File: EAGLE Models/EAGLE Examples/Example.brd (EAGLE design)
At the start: 160 x 100 mm, 2 parts

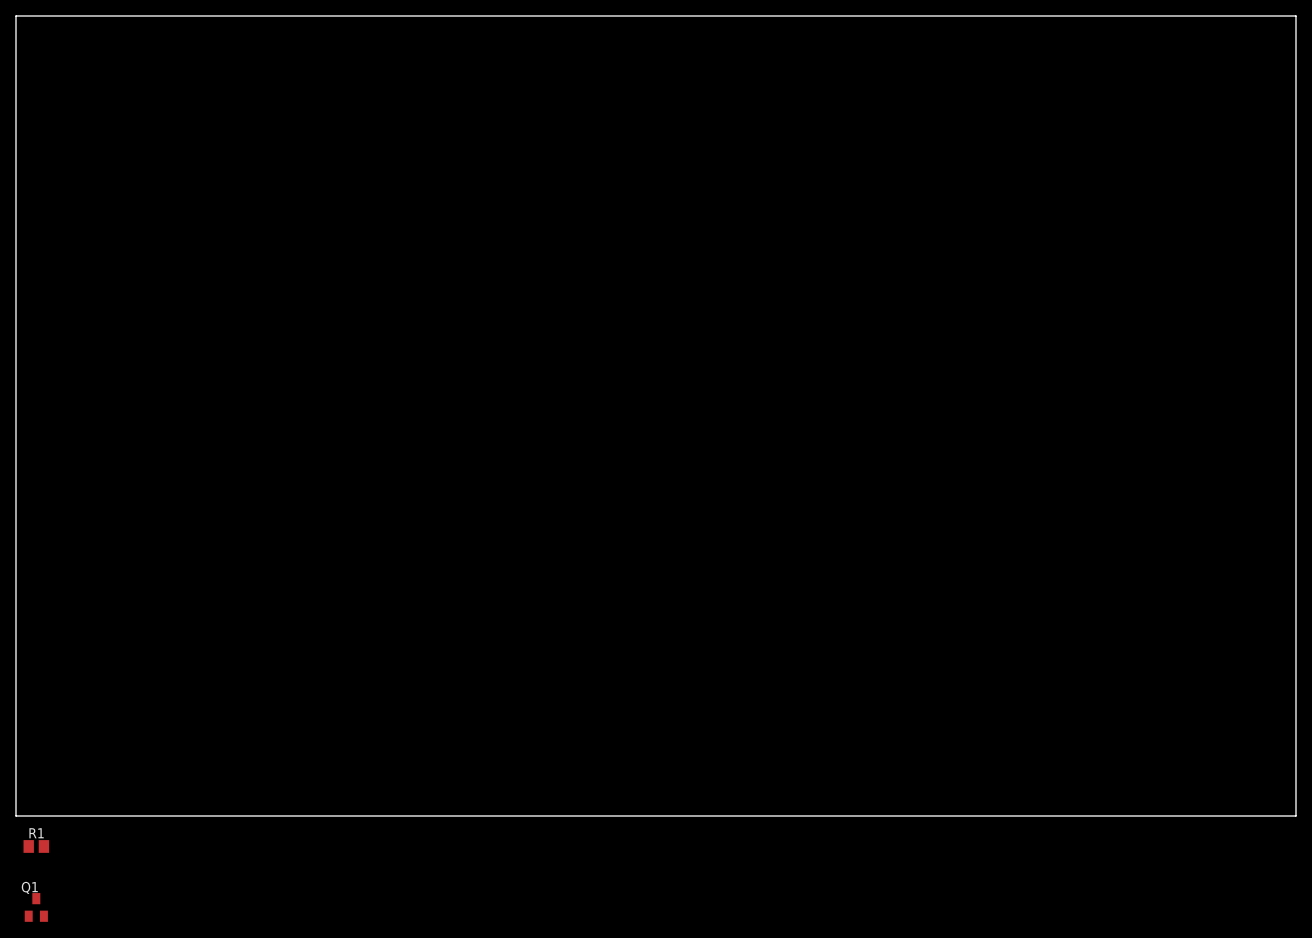
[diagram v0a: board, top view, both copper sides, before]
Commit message: Finished Example board for EAGLE tutorial
Did board layout
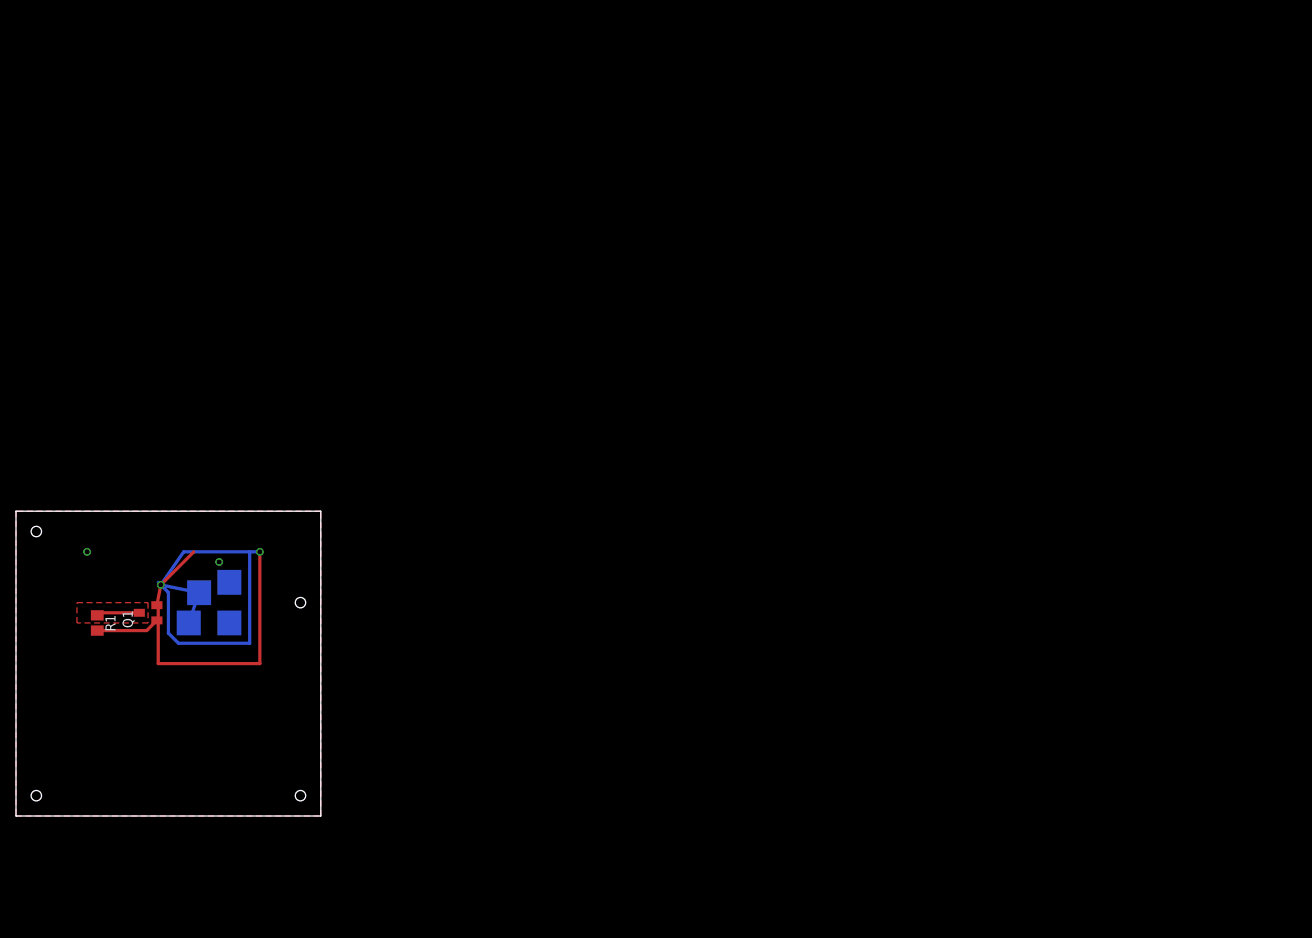
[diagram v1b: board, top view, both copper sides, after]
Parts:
- added D1: OVSA1BBC, TTelectronics:4-PLCC
- moved Q1 39.4 mm to (16.5, 25.4), turned to 90 degrees
- moved R1 29.0 mm to (10.2, 24.1), turned to 270 degrees
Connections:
- net N$1 renamed GATE
- removed net N$2: Q1.3
- removed net N$3: Q1.2
- new net DRIN: D1.1, D1.2, Q1.2
- new net GND: D1.3, D1.4
- new net VCC: Q1.3, R1.1
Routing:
- net DRIN: track 0.00 -> 95.1 mm, vias 0 -> 2
- net GATE: track 0.00 -> 7.98 mm
- net VCC: track 0.00 -> 5.38 mm
- added copper zone on layer 1, net GND
- added copper zone on layer 16, net GND
- added copper zone on layer 1, net VCC
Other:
- board size 160 x 100 mm -> 38.1 x 38.1 mm
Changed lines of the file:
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@@
 <layer number="43" name="vRestrict" color="2" fill="10" visible="yes" active="yes"/>
 <layer number="44" name="Drills" color="7" fill="1" visible="no" active="yes"/>
-<layer number="45" name="Holes" color="7" fill="1" visible="no" active="yes"/>
+<layer number="45" name="Holes" color="7" fill="1" visible="yes" active="yes"/>
 <layer number="46" name="Milling" color="3" fill="1" visible="no" active="yes"/>
 <layer number="47" name="Measures" color="7" fill="1" visible="no" active="yes"/>
@@
 <board>
 <plain>
-<wire x1="0" y1="0" x2="160" y2="0" width="0" layer="20"/>
-<wire x1="160" y1="0" x2="160" y2="100" width="0" layer="20"/>
-<wire x1="160" y1="100" x2="0" y2="100" width="0" layer="20"/>
-<wire x1="0" y1="100" x2="0" y2="0" width="0" layer="20"/>
+<wire x1="0" y1="0" x2="38.1" y2="0" width="0" layer="20"/>
+<wire x1="38.1" y1="0" x2="38.1" y2="38.1" width="0" layer="20"/>
+<wire x1="38.1" y1="38.1" x2="0" y2="38.1" width="0" layer="20"/>
+<wire x1="0" y1="38.1" x2="0" y2="0" width="0" layer="20"/>
+<hole x="2.54" y="35.56" drill="1.3"/>
+<hole x="2.54" y="2.54" drill="1.3"/>
+<hole x="35.56" y="2.54" drill="1.3"/>
+<hole x="35.56" y="26.67" drill="1.3"/>
 </plain>
 <attributes>
@@
 </autorouter>
 <elements>
-<element name="R1" library="adafruit" package="M0805" value="5K" x="2.54" y="-3.81"/>
-<element name="Q1" library="adafruit" package="SOT23" value="" x="2.54" y="-11.43"/>
+<element name="R1" library="adafruit" package="M0805" value="5K" x="10.16" y="24.13" rot="R270"/>
+<element name="Q1" library="adafruit" package="SOT23" value="" x="16.51" y="25.4" rot="R90"/>
+<element name="D1" library="TTelectronics" package="4-PLCC" value="OVSA1BBC" x="24.13" y="26.67" rot="MR270"/>
 </elements>
 <signals>
-<signal name="N$1">
+<signal name="GATE">
 <contactref element="R1" pad="2"/>
 <contactref element="Q1" pad="1"/>
-<wire x1="3.49" y1="-3.81" x2="1.59" y2="-12.53" width="0" layer="19" extent="1-1"/>
+<wire x1="10.16" y1="23.18" x2="16.34" y2="23.18" width="0.4064" layer="1"/>
+<wire x1="16.34" y1="23.18" x2="17.61" y2="24.45" width="0.4064" layer="1"/>
 </signal>
-<signal name="N$2">
+<signal name="DRIN">
+<contactref element="Q1" pad="2"/>
+<contactref element="D1" pad="2"/>
+<contactref element="D1" pad="1"/>
+<wire x1="17.61" y1="26.35" x2="18.1" y2="28.89" width="0.4064" layer="1"/>
+<wire x1="18.1" y1="28.89" x2="22.89" y2="27.91" width="0.4064" layer="16"/>
+<wire x1="22.89" y1="27.91" x2="21.59" y2="24.13" width="0.4064" layer="16"/>
+<via x="18.1" y="28.89" extent="1-16" drill="0.6" shape="square"/>
+<wire x1="18.1" y1="28.89" x2="22.23" y2="33.02" width="0.4064" layer="1"/>
+<wire x1="30.48" y1="33.02" x2="30.48" y2="19.05" width="0.4064" layer="1"/>
+<wire x1="30.48" y1="19.05" x2="17.78" y2="19.05" width="0.4064" layer="1"/>
+<wire x1="17.78" y1="19.05" x2="17.78" y2="26.67" width="0.4064" layer="1"/>
+<wire x1="18.1" y1="28.89" x2="20.96" y2="33.02" width="0.4064" layer="16"/>
+<wire x1="20.96" y1="33.02" x2="29.21" y2="33.02" width="0.4064" layer="16"/>
+<wire x1="29.21" y1="33.02" x2="29.21" y2="21.59" width="0.4064" layer="16"/>
+<wire x1="29.21" y1="21.59" x2="20.32" y2="21.59" width="0.4064" layer="16"/>
+<wire x1="20.32" y1="21.59" x2="19.05" y2="22.86" width="0.4064" layer="16"/>
+<wire x1="19.05" y1="22.86" x2="19.05" y2="27.94" width="0.4064" layer="16"/>
+<wire x1="19.05" y1="27.94" x2="17.78" y2="29.21" width="0.4064" layer="16"/>
+<via x="30.48" y="33.02" extent="1-16" drill="0.6"/>
+<wire x1="30.48" y1="33.02" x2="29.21" y2="33.02" width="0.4064" layer="16"/>
+</signal>
+<signal name="GND">
+<contactref element="D1" pad="4"/>
+<contactref element="D1" pad="3"/>
+<polygon width="0.4064" layer="1" rank="6">
+<vertex x="0" y="0"/>
+<vertex x="38.1" y="0"/>
+<vertex x="38.1" y="38.1"/>
+<vertex x="0" y="38.1"/>
+</polygon>
+<polygon width="0.4064" layer="16" isolate="1.016">
+<vertex x="0" y="0"/>
+<vertex x="38.1" y="0"/>
+<vertex x="38.1" y="38.1"/>
+<vertex x="0" y="38.1"/>
+</polygon>
+<via x="8.89" y="33.02" extent="1-16" drill="0.6"/>
+<via x="25.4" y="31.75" extent="1-16" drill="0.6"/>
+</signal>
+<signal name="VCC">
+<contactref element="R1" pad="1"/>
 <contactref element="Q1" pad="3"/>
-</signal>
-<signal name="N$3">
-<contactref element="Q1" pad="2"/>
+<wire x1="15.41" y1="25.4" x2="10.48" y2="25.4" width="0.4064" layer="1"/>
+<wire x1="10.48" y1="25.4" x2="10.16" y2="25.08" width="0.4064" layer="1"/>
+<polygon width="0.4064" layer="1">
+<vertex x="7.62" y="26.67"/>
+<vertex x="16.51" y="26.67"/>
+<vertex x="16.51" y="24.13"/>
+<vertex x="7.62" y="24.13"/>
+</polygon>
 </signal>
 </signals>
+<errors>
+</errors>
 </board>
 </drawing>
